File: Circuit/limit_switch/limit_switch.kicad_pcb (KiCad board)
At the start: 2 copper layers, 39.5 x 31.4 mm, 12 parts

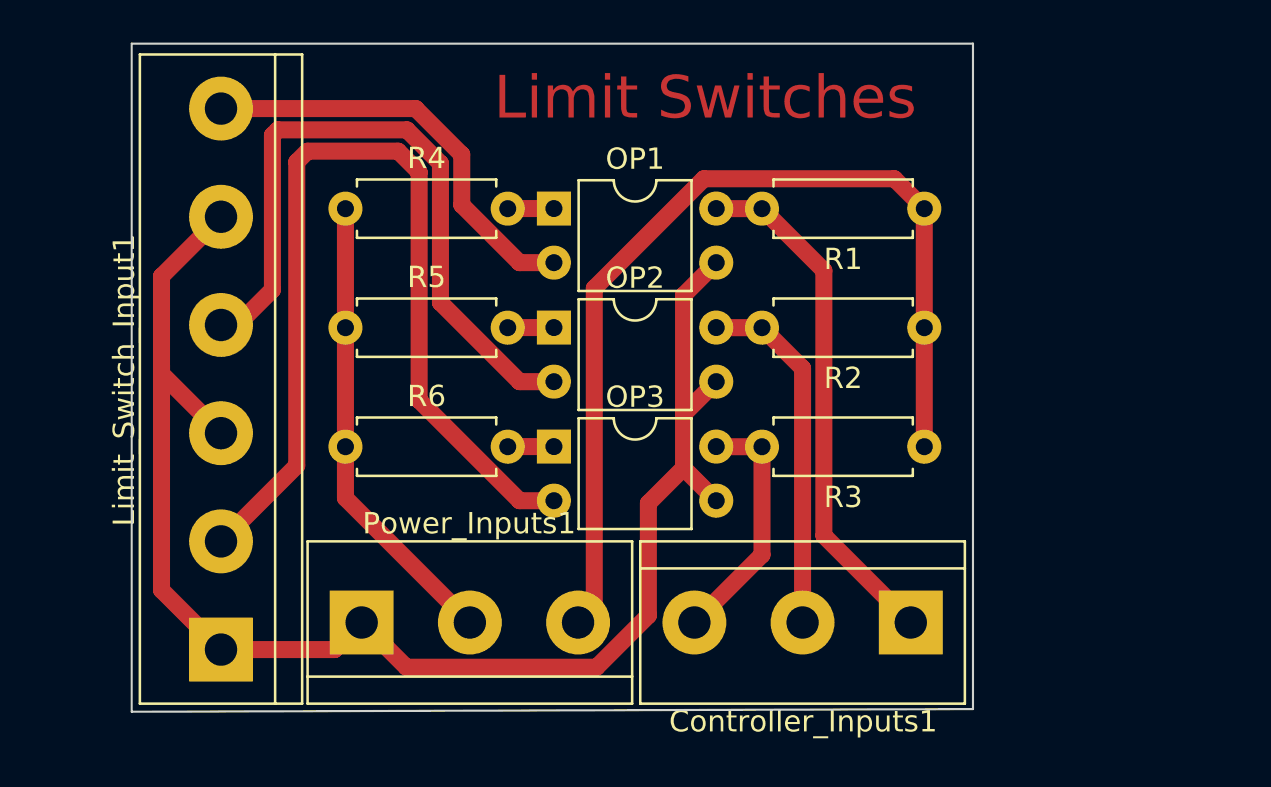
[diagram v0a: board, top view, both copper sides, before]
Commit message: Finished limit switch circuit and minor changes to cam module
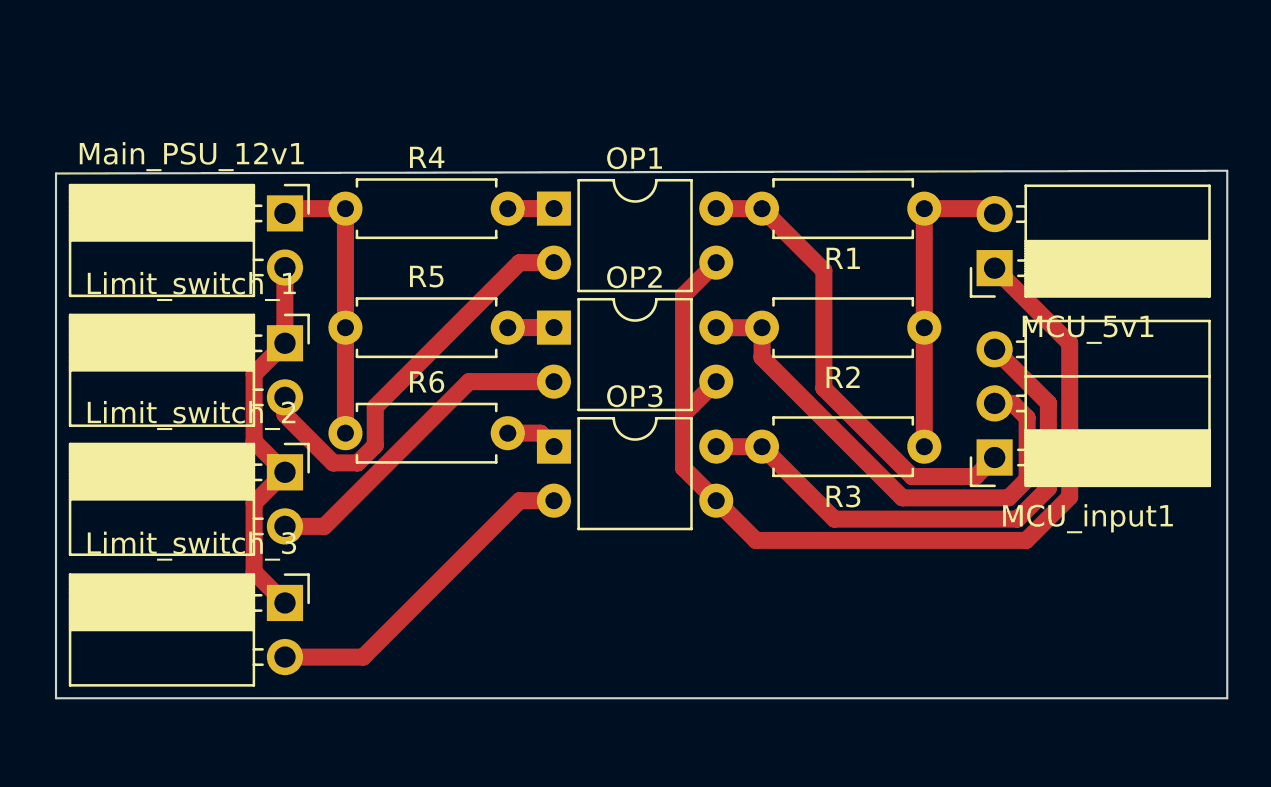
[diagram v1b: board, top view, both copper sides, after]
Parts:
- removed Controller_Inputs1, Power_Inputs1: Screw_Terminal_01x03, TerminalBlock:TerminalBlock_bornier-3_P5.08mm
- removed Limit_Switch_Input1: Screw_Terminal_01x06, TerminalBlock:TerminalBlock_bornier-6_P5.08mm
- added Limit_switch_1: Conn_01x02_Socket, Connector_PinSocket_2.54mm:PinSocket_1x02_P2.54mm_Horizontal, F.Cu at (124.0, 105.5)
- added Limit_switch_2: Conn_01x02_Socket, Connector_PinSocket_2.54mm:PinSocket_1x02_P2.54mm_Horizontal, F.Cu at (124.0, 111.6)
- added Limit_switch_3: Conn_01x02_Socket, Connector_PinSocket_2.54mm:PinSocket_1x02_P2.54mm_Horizontal, F.Cu at (124.0, 117.7)
- added MCU_5v1: Conn_01x02_Socket, Connector_PinSocket_2.54mm:PinSocket_1x02_P2.54mm_Horizontal, F.Cu at (157.4, 102.0)
- added MCU_input1: Conn_01x03_Socket, Connector_PinSocket_2.54mm:PinSocket_1x03_P2.54mm_Horizontal, F.Cu at (157.4, 110.9)
- added Main_PSU_12v1: Conn_01x02_Socket, Connector_PinSocket_2.54mm:PinSocket_1x02_P2.54mm_Horizontal, F.Cu at (124.0, 99.4)
- moved R6 0.64 mm to (126.9, 109.7)
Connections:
- net +5VA renamed +12V
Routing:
- net +5V: track 45.4 -> 14.6 mm
- net Net-(Limit_switch_3-Pin_2): track 44.6 -> 15.7 mm
- net GND: track 71.7 -> 45.0 mm
- net GNDA: track 0.00 -> 18.2 mm
- net Net-(Limit_switch_2-Pin_2): track 32.4 -> 15.4 mm
- net Net-(MCU_input1-Pin_3): track 11.7 -> 25.2 mm
- net +12V: track 21.9 -> 13.5 mm
- net Net-(MCU_input1-Pin_2): track 16.8 -> 23.8 mm
- net Net-(MCU_input1-Pin_1): track 24.5 -> 21.9 mm
- net Net-(Limit_switch_1-Pin_2): track 20.0 -> 19.3 mm
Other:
- board size 39.5 x 31.4 mm -> 55 x 24.8 mm
- board text removed: "Limit Switches"

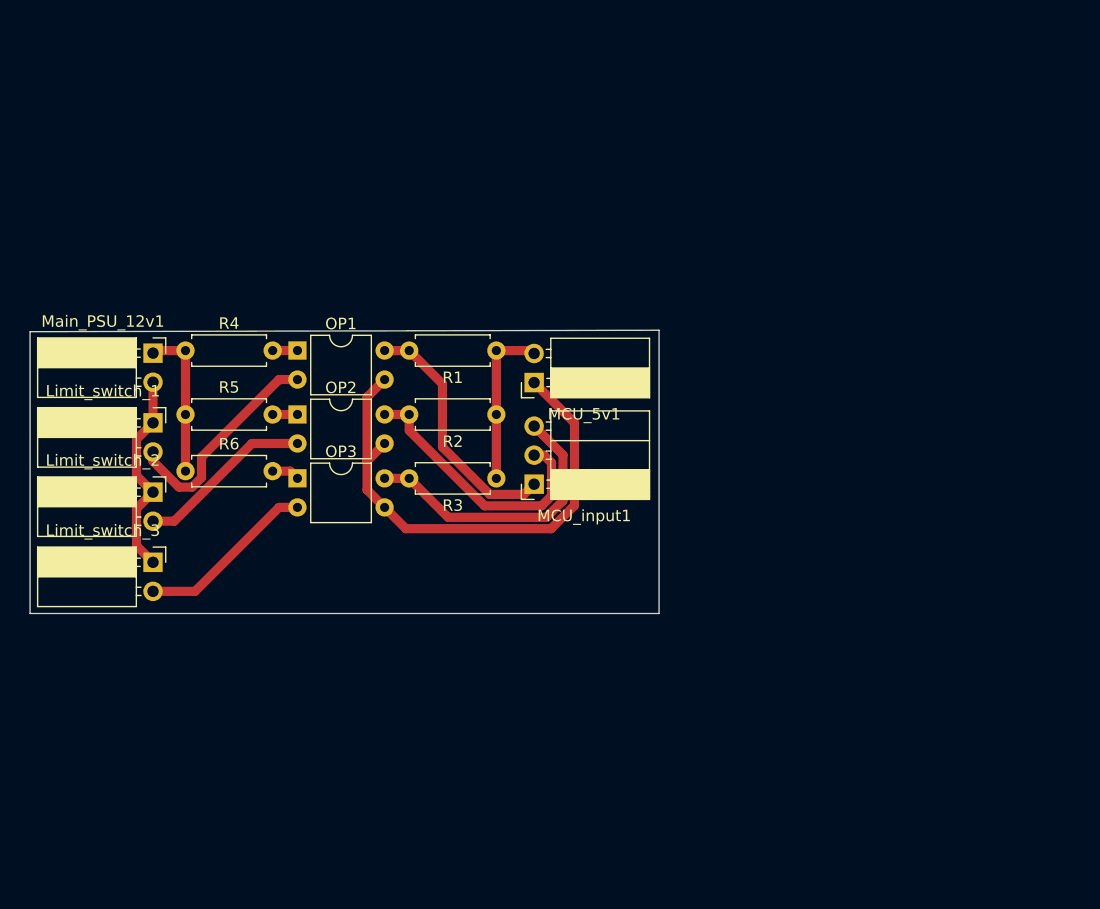
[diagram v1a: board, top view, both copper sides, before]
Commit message: added passive filters to limit switch circuit
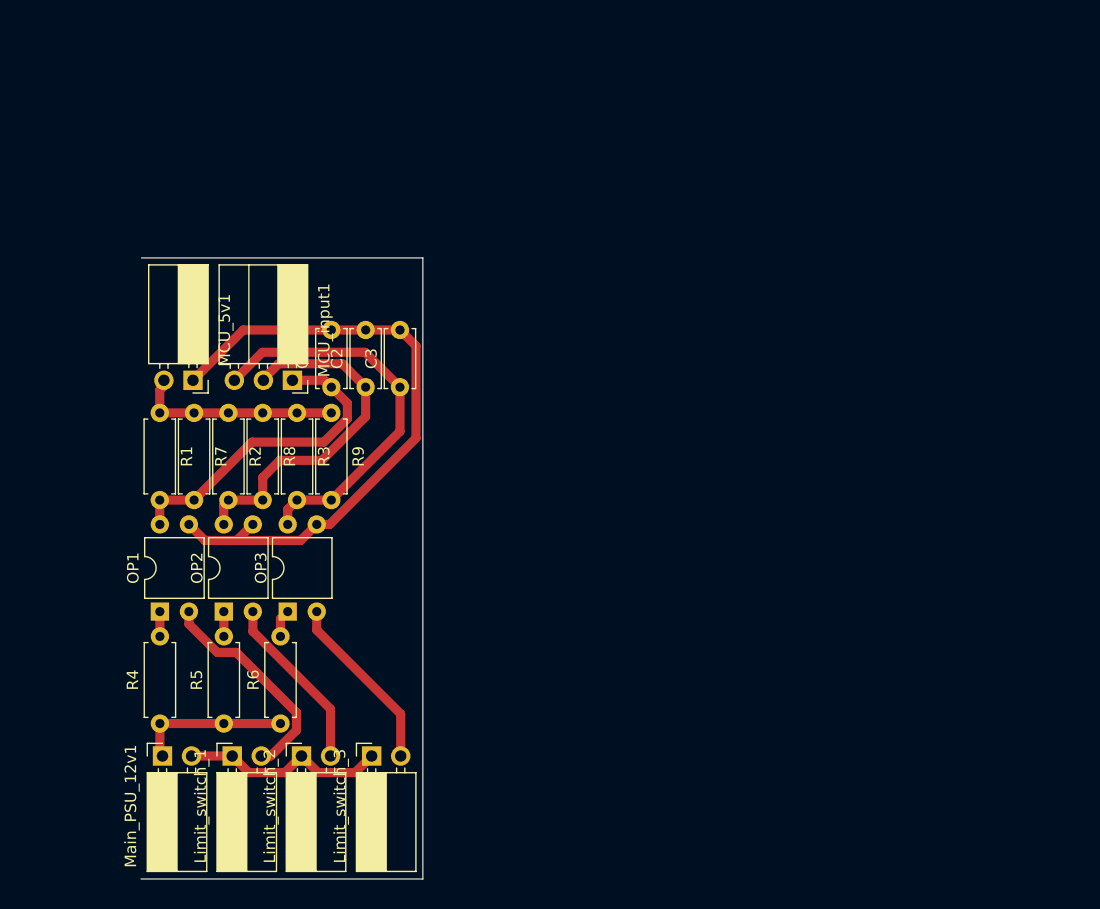
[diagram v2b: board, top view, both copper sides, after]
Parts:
- added C1: 0.1uF, Capacitor_THT:C_Disc_D5.0mm_W2.5mm_P5.00mm, F.Cu at (139.6, 102.4)
- added C2: 0.1uF, Capacitor_THT:C_Disc_D5.0mm_W2.5mm_P5.00mm, F.Cu at (142.6, 102.4)
- added C3: 0.1uF, Capacitor_THT:C_Disc_D5.0mm_W2.5mm_P5.00mm, F.Cu at (145.6, 102.4)
- added R7: 1k, Resistor_THT:R_Axial_DIN0207_L6.3mm_D2.5mm_P7.62mm_Horizontal, F.Cu at (127.6, 104.6)
- added R8: 1k, Resistor_THT:R_Axial_DIN0207_L6.3mm_D2.5mm_P7.62mm_Horizontal, F.Cu at (133.6, 104.6)
- added R9: 1k, Resistor_THT:R_Axial_DIN0207_L6.3mm_D2.5mm_P7.62mm_Horizontal, F.Cu at (139.6, 104.6)
- moved Main_PSU_12v1 35.2 mm to (124.9, 134.6), turned to 90 degrees
- moved R4 32.7 mm to (124.6, 131.8), turned to 90 degrees
- moved Limit_switch_1 29.9 mm to (131.0, 134.6), turned to 90 degrees
- moved R1 29.9 mm to (124.6, 104.6), turned to -90 degrees
- moved MCU_5v1 29.8 mm to (127.5, 101.8), turned to -90 degrees
- moved R5 27.2 mm to (130.2, 131.8), turned to 90 degrees
- moved Limit_switch_2 26.5 mm to (137.0, 134.6), turned to 90 degrees
- moved OP1 25.8 mm to (124.6, 122.0), turned to 90 degrees
- moved Limit_switch_3 25.5 mm to (143.1, 134.6), turned to 90 degrees
- moved R6 23.6 mm to (135.2, 131.8), turned to 90 degrees
- moved R2 23.4 mm to (130.6, 104.6), turned to -90 degrees
- moved MCU_input1 23.0 mm to (136.2, 101.8), turned to -90 degrees
- moved OP2 18.4 mm to (130.2, 122.0), turned to 90 degrees
- moved R3 18.3 mm to (136.6, 104.6), turned to -90 degrees
- moved OP3 11.7 mm to (135.8, 122.0), turned to 90 degrees
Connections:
- net Net-(MCU_input1-Pin_1) renamed limit_switch_MCU1
- net Net-(MCU_input1-Pin_2) renamed limit_switch_MCU2
- net Net-(MCU_input1-Pin_3) renamed limit_switch_MCU3
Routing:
- net GND: track 45.0 -> 56.1 mm
- net limit_switch_MCU3: track 25.2 -> 34.6 mm
- net limit_switch_MCU2: track 23.8 -> 31.5 mm
- net limit_switch_MCU1: track 21.9 -> 28.5 mm
- net +5V: track 14.6 -> 18.0 mm
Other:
- board size 55 x 24.8 mm -> 24.6 x 54.3 mm

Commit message: Implemented Isolators in PWM Mutliplexer
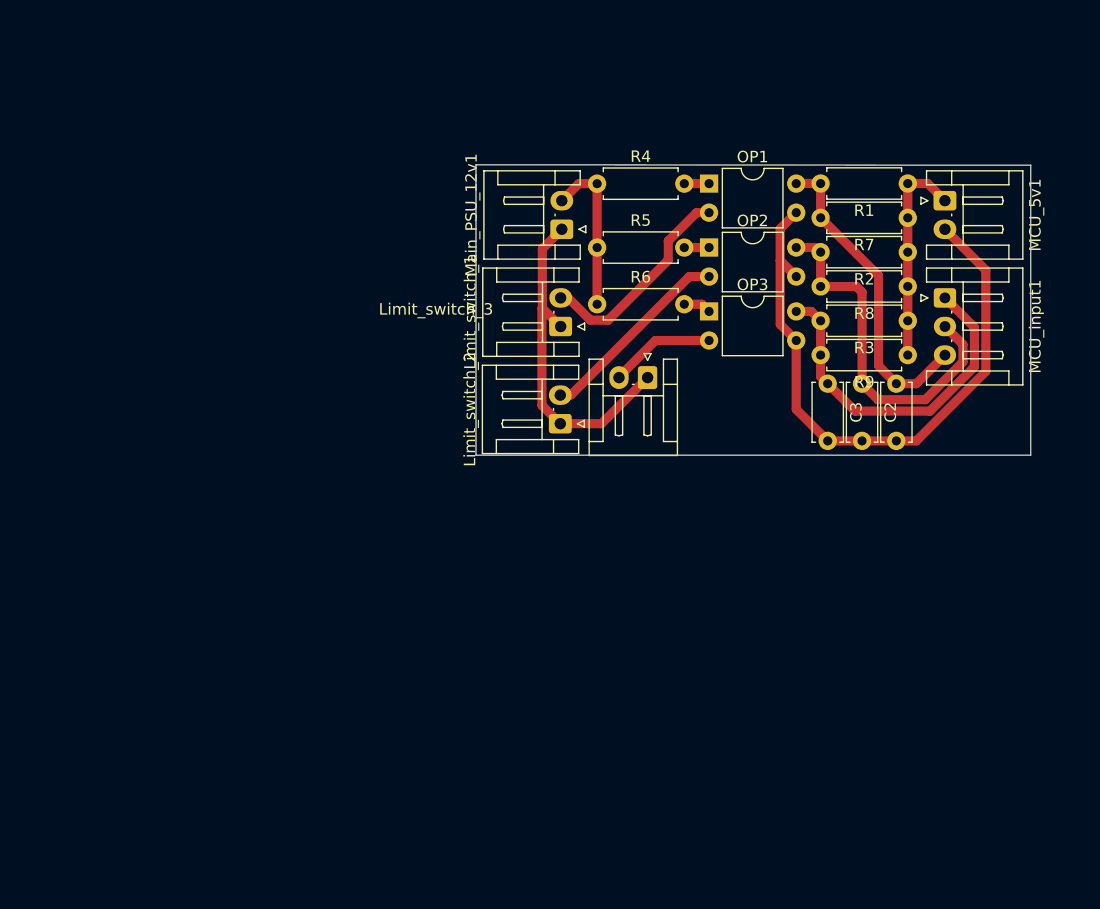
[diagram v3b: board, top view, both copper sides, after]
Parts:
- Limit_switch_1, Limit_switch_2, Limit_switch_3, MCU_5v1, Main_PSU_12v1: footprint Connector_PinSocket_2.54mm:PinSocket_1x02_P2.54mm_Horizontal -> Connector_JST:JST_EH_S2B-EH_1x02_P2.50mm_Horizontal
- MCU_input1: footprint Connector_PinSocket_2.54mm:PinSocket_1x03_P2.54mm_Horizontal -> Connector_JST:JST_EH_S3B-EH_1x03_P2.50mm_Horizontal
- moved R1 68.4 mm to (190.0, 84.6), turned to 180 degrees
- moved MCU_5v1 67.6 mm to (193.3, 86.1)
- moved R7 64.7 mm to (190.0, 87.6), turned to 180 degrees
- moved R2 61.0 mm to (190.0, 90.6), turned to 180 degrees
- moved OP1 60.9 mm to (172.7, 84.6), turned to 0 degrees
- moved R4 60.7 mm to (162.9, 84.6), turned to 0 degrees
- moved Main_PSU_12v1 57.8 mm to (159.8, 88.6)
- moved MCU_input1 57.5 mm to (193.3, 94.6)
- moved R8 57.5 mm to (190.0, 93.6), turned to 180 degrees
- moved R3 54.0 mm to (190.0, 96.6), turned to 180 degrees
- moved OP2 53.0 mm to (172.7, 90.2), turned to 0 degrees
- moved R5 52.9 mm to (162.9, 90.2), turned to 0 degrees
- moved R9 50.7 mm to (190.0, 99.6), turned to 180 degrees
- moved C1 49.4 mm to (189.0, 102.1), turned to -90 degrees
- moved Limit_switch_1 47.3 mm to (159.7, 97.1)
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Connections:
- MCU_5v1 pad 1: GND -> +5V
- MCU_5v1 pad 2: +5V -> GND
- MCU_input1 pad 1: limit_switch_MCU1 -> limit_switch_MCU3
- MCU_input1 pad 3: limit_switch_MCU3 -> limit_switch_MCU1
- Main_PSU_12v1 pad 1: +12V -> GNDA
- Main_PSU_12v1 pad 2: GNDA -> +12V
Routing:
- net GNDA: track 18.2 -> 29.9 mm
- net Net-(Limit_switch_3-Pin_2): track 15.7 -> 9.26 mm
- net limit_switch_MCU3: track 34.6 -> 30.7 mm
- net Net-(Limit_switch_2-Pin_2): track 15.4 -> 17.3 mm
- net GND: track 56.1 -> 54.5 mm
- net +5V: track 18.0 -> 18.9 mm
- net limit_switch_MCU1: track 28.5 -> 27.7 mm
- net +12V: track 13.5 -> 14.2 mm
- net Net-(Limit_switch_1-Pin_2): track 19.3 -> 18.7 mm
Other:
- board size 24.6 x 54.3 mm -> 48.5 x 25.4 mm

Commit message: DC Motor Driver Circuit fine tuning for manufacturing
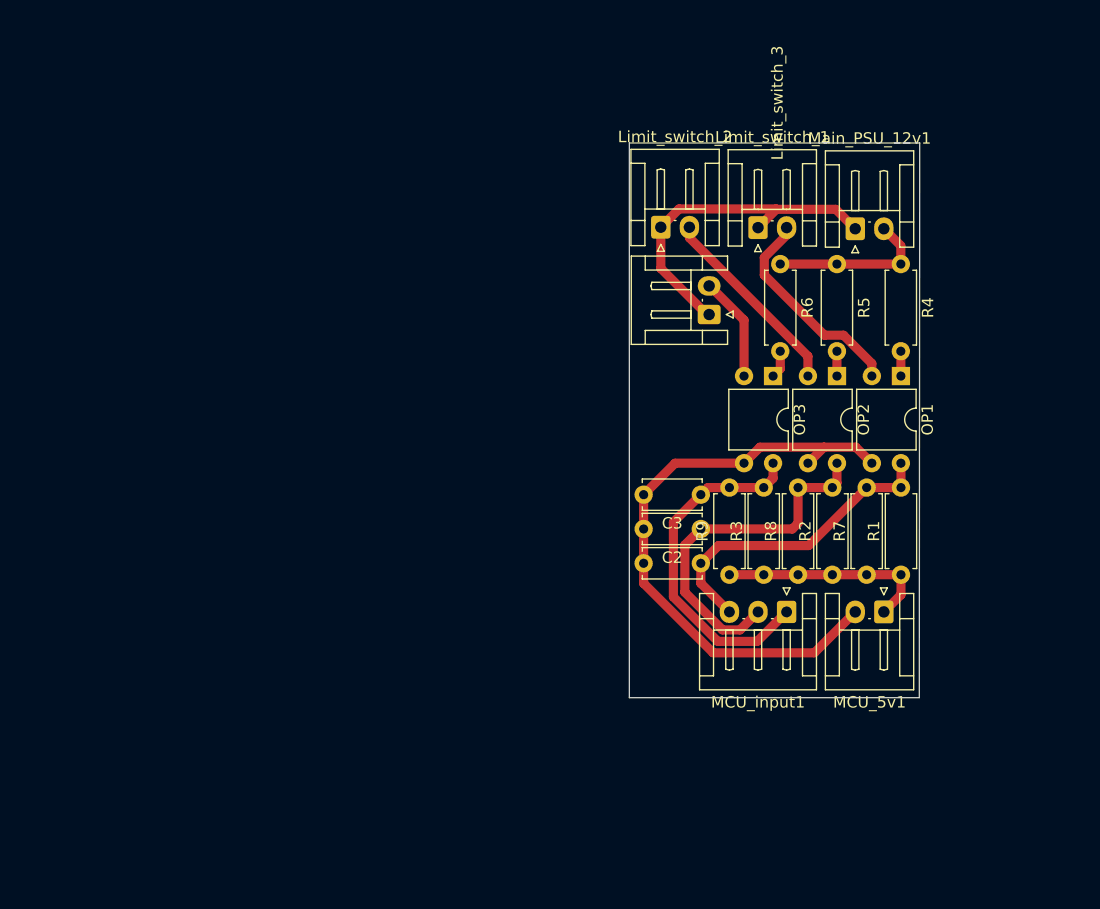
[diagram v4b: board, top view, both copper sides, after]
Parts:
- moved MCU_5v1 36.3 mm to (187.9, 122.0), turned to 180 degrees
- moved R1 34.2 mm to (189.4, 118.8), turned to 90 degrees
- moved R7 31.4 mm to (186.4, 118.8), turned to 90 degrees
- moved MCU_input1 30.7 mm to (179.4, 122.0), turned to 180 degrees
- moved R2 29.0 mm to (183.4, 118.8), turned to 90 degrees
- moved R4 27.5 mm to (189.4, 91.6), turned to -90 degrees
- moved R8 27.0 mm to (180.4, 118.8), turned to 90 degrees
- moved Main_PSU_12v1 25.7 mm to (185.4, 88.5), turned to 0 degrees
- moved R3 25.5 mm to (177.4, 118.8), turned to 90 degrees
- moved R9 24.7 mm to (174.4, 118.8), turned to 90 degrees
- moved OP1 23.8 mm to (189.4, 101.4), turned to -90 degrees
- moved C1 23.2 mm to (171.9, 117.8), turned to 180 degrees
- moved R5 21.0 mm to (183.8, 91.6), turned to -90 degrees
- moved Limit_switch_1 19.3 mm to (176.9, 88.4), turned to 0 degrees
- moved Limit_switch_2 19.3 mm to (168.4, 88.4), turned to 0 degrees
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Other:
- board size 48.5 x 25.4 mm -> 25.4 x 48.5 mm

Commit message: further development in esp32-cam
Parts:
- moved MCU_5v1 36.4 mm to (195.9, 86.5), turned to -90 degrees
- moved R1 33.9 mm to (192.6, 85.0), turned to 180 degrees
- moved MCU_input1 31.6 mm to (195.9, 95.0), turned to -90 degrees
- moved R7 31.4 mm to (192.6, 88.0), turned to 180 degrees
- moved R2 29.2 mm to (192.6, 91.0), turned to 180 degrees
- moved R8 27.6 mm to (192.6, 94.0), turned to 180 degrees
- moved R3 26.5 mm to (192.6, 97.0), turned to 180 degrees
- moved R9 26.1 mm to (192.6, 100.0), turned to 180 degrees
- moved C1 24.9 mm to (191.6, 102.5), turned to -90 degrees
- moved R4 24.8 mm to (165.5, 85.0), turned to 0 degrees
- moved Main_PSU_12v1 23.1 mm to (162.4, 89.0), turned to 90 degrees
- moved OP1 21.7 mm to (175.2, 85.0), turned to 0 degrees
- moved C2 20.7 mm to (188.6, 102.5), turned to -90 degrees
- moved Limit_switch_2 18.7 mm to (162.2, 106.0), turned to 90 degrees
- moved R5 18.4 mm to (165.5, 90.6), turned to 0 degrees
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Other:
- board size 25.4 x 48.5 mm -> 48.5 x 25.4 mm
